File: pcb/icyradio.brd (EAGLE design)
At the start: 100 x 100 mm, 142 parts, among them J1 TRSJACK, J2 TRSJACK, J3 TRSJACK, U1 ICE40HX8K-CT256, U10 ATSAMS70Q21B-C, U2 EFM32GG11B820F2048GL120, U3 LTC2206, U4 CP2615, U5 DSC1211DE3-C0017, U6 TSCS25A3X1NDGXZAX, U7 MIC5301-1.8YD5, U8 MIC23159, U9 RT820T2, X1 8 MHz, X2 32.768 kHz, X3 DNP

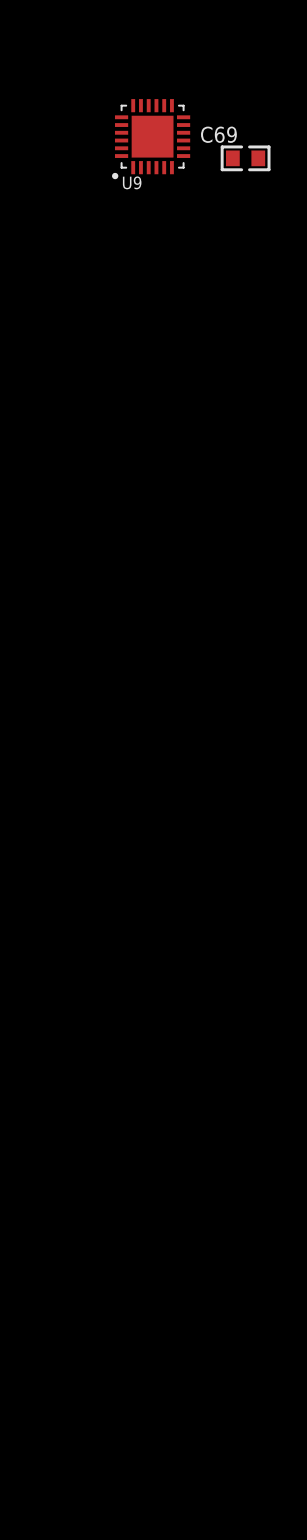
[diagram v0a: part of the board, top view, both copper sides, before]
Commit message: Added SPI slave with lots of registers Changed some names and comments Added IRQ logic
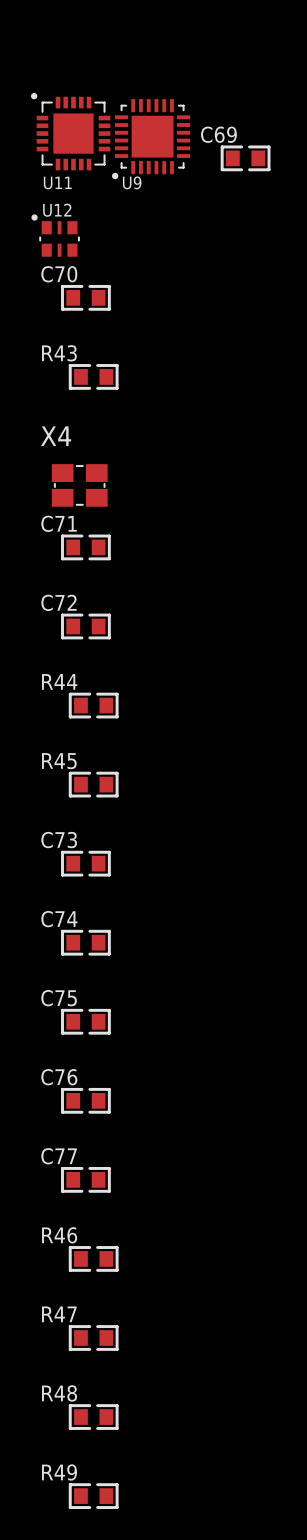
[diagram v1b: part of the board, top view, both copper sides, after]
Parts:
- added C70, C73, C74, C75, C76, C77: 100nF, Capacitor:CAP0603
- added C71, C72: DNP, Capacitor:CAP0603
- added R43, R44, R45: 100K Ohms, Resistor:RES0603
- added R46, R47, R48, R49: 0 Ohms, Resistor:RES0603
- added U11: SI5351C, Silicon Labs:QFN20
- added U12: DSC1201DE3-50M00000, Microchip:VDFN6
- added X4: DNP, Crystal:4-SMD-3225
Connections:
- new net !CLK_MNGR_IRQ: R45.1, U11.3
- new net !CLK_MNGR_OE: R44.1, U11.7
- new net !CLK_MNGR_REFCLK_STDBY: R43.2, U12.1
- new net DDC_CLK: R49.1
- new net FPGA_GP_CLK1: R48.1
- new net FPGA_GP_CLK2: R47.1
- new net MCU_MAIN_CLK: R46.1
- new net N$60: U11.6, U12.4
- new net N$61: C71.1, U11.2, X4.4
- new net N$62: C72.1, U11.1, X4.2
- net 3V3: now also C70.1, C73.1, C74.1, C75.1, C76.1, C77.1, R44.2, R45.2, U11.10, U11.11, U11.14, U11.18, U11.20, U12.6
- net GND: now also C70.2, C71.2, C72.2, C73.2, C74.2, C75.2, C76.2, C77.2, R43.1, U11.21, U12.3, X4.1, X4.3

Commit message: Add testbenches Change toolchain flow
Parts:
- added C100, C101, C102, C103, C98, C99: 220pF, Capacitor:CAP0603
- added C104, C105, C106, C108, C109, C111, C112, C113, C117, C121, C122, C126, C128, C131, C78, C79, C80, C81, C82, C83, C97: 100nF, Capacitor:CAP0603
- added C107, C110: DNP, Capacitor:CAP0603
- added C114, C115, C129, C133, C134, C140, C141, C84, C87, C88: 4.7uF, Capacitor:CAP0603
- added C116, C119, C124: 470pF, Capacitor:CAP0603
- added C118, C123, C125, C127: 100uF, Capacitor:CAP1206
- added C120, C130, C85, C86: 10nF, Capacitor:CAP0603
- added C132, C135, C136, C138, C139, C89, C90, C91, C92, C95, C96: 1uF, Capacitor:CAP0603
- added C137: 10uF, Capacitor:CAP0603
- added C93, C94: 22nF, Capacitor:CAP0603
- added L10, L11, L12, L7, L8, L9: 1.3uH, Inductor:IND0603
- added L13, L14: (no value), Inductor:IND0603
- added L15, L16, L17, L18: 2.7nH, Inductor:IND0603
- added L19: 2.2uH, Inductor:IND0805
- added L20, L22: 2.2uH, Inductor:IND2520
- added L21: 350nH, Inductor:IND0805
- added L23: 350nH, Inductor:IND0603
- added R50, R51, R62, R63, R66, R69, R71, R72, R73: 100K Ohms, Resistor:RES0603
- added R52, R53, R54, R55, R56, R57: 0 Ohms, Resistor:RES0603
- added R58, R59: 5.1K Ohms, Resistor:RES0603
- added R60: 274K Ohms, Resistor:RES0603
- added R61: 294K Ohms, Resistor:RES0603
- added R64, R67: 309K Ohms, Resistor:RES0603
- added R65: 64.9K Ohms, Resistor:RES0603
- added R68: 71.5K Ohms, Resistor:RES0603
- added R70: 820 Ohms, Resistor:RES0603
- added RFCON2: RFCON-SMA-EDGE, RF Connector:SMA-EDGE
- added RFCON3: RFCON-U.FL, RF Connector:U.FL
- added U13: DSC1201DE3-50M00000, Microchip:VDFN6
- added U14: SI5351C, Silicon Labs:QFN20
- added U15: MIC23155, Microchip:DFN10
- added U16: MIC23159, Microchip:VQFN20
- added U17: MIC2019, Microchip:SOT23-6
- added U18: ADP150UJZ-1.8, Analog Devices:SOT23-5
- added U19: ADP150UJZ-3.3, Analog Devices:SOT23-5
- added U20, U21: MIC94305, Microchip:DFN6
- C10: value 4.7uF -> 2.2uF
- C11, C56: value 10nF -> 100nF
- C12: value 1uF -> 12pF
- C13: value 100nF -> 12pF
- C14: value 330pF -> 12pF
- C15: value 6.8nF -> 1uF
- C17, C18: value DNP -> 100nF
- C19: value 100nF -> 6.8nF
- C2, C3, C4: value 12pF -> 100nF
- C21: value 100nF -> 2.2uF
- C24, C28: value 100nF -> 330pF
- C29: value 2.2uF -> 10nF
- C30, C42, C55, C57: value 1uF -> 100nF
- C33: value 100nF -> 1uF
- C37, C38, C39, C58: value 4.7uF -> 100nF
- C41: value 10nF -> 100pF
- C43, C44, C51, C52: value 220pF -> 200pF
- C45, C46: value 1uF -> 200pF
- C47, C50: value 1uF -> 620pF
- C48, C49: value 220pF -> 620pF
- C53, C54: value 22nF -> 200pF
- C6: value 2.2uF -> 100nF
- C60, C66: value 100uF -> 100nF; device Capacitor:CAP1206 -> Capacitor:CAP0603
- C61: value 470pF -> 10nF
- C62: value 470pF -> 100nF
- C63: value 4.7uF -> 10pF
- C65, C67: value 100nF -> 10pF
- C68: value 100uF -> 0.4pF; device Capacitor:CAP1206 -> Capacitor:CAP0603
- C69, C75, C76: value 100nF -> 0.4pF
- C70: value 100nF -> 2.7nF
- C71: value DNP -> 39nF
- C72: value DNP -> 1.3pF
- C73: value 100nF -> 1.3pF
- C74: value 100nF -> 1.2nF
- C8: value 100nF -> DNP
- C9: value 330pF -> DNP
- L1: value 4.7uH -> 150nH
- L3: value 150nH -> 8.2nH
- L4: value 8.2nH -> 680nH
- L5: value 2.2uH -> 1.3uH; device Inductor:IND0805 -> Inductor:IND0603
- L6: value 2.2uH -> 1.3uH; device Inductor:IND2520 -> Inductor:IND0603
- R1: value 25 Ohms -> 100K Ohms
- R11: value 1K Ohms -> 220 Ohms
- R12: value 10K Ohms -> 220 Ohms
- R13: value 5.1K Ohms -> 100K Ohms
- R14: value 5.1K Ohms -> 1.5K Ohms
- R15: value 47K Ohms -> 50 Ohms
- R16: value 24K Ohms -> 50 Ohms
- R17, R18: value 10K Ohms -> 50 Ohms
- R2: value 25 Ohms -> 0 Ohms
- R20: value 4.7K Ohms -> 10K Ohms
- R21, R22: value 600 Ohms -> 100 Ohms
- R23: value 4.7K Ohms -> 100K Ohms
- R24: value 2.21K Ohms -> 4.7K Ohms
- R25: value 2.21K Ohms -> 100 Ohms
- R26: value 4.7K Ohms -> 360 Ohms
- R27: value 600 Ohms -> 680 Ohms
- R28: value 600 Ohms -> 5.1K Ohms
- R29: value 4.7K Ohms -> 5.1K Ohms
- R3: value 25 Ohms -> 1K Ohms
- R30: value 3.57 Ohms -> 10K Ohms
- R31: value 3.57 Ohms -> 24K Ohms
- R32: value 100 Ohms -> 47K Ohms
- R33: value 100 Ohms -> 10K Ohms
- R34: value 309K Ohms -> 100 Ohms
- R35: value 71.5K Ohms -> 2.21K Ohms
- R36, R40: value 100K Ohms -> 4.7K Ohms
- R37: value 274K Ohms -> 4.7K Ohms
- R38: value 294K Ohms -> 10K Ohms
- R39: value 100K Ohms -> 2.21K Ohms
- R41: value 5.1K Ohms -> 4.7K Ohms
- R42: value 5.1K Ohms -> 100 Ohms
- R43, R44: value 100K Ohms -> 600 Ohms
- R45: value 100K Ohms -> 3.57 Ohms
- R46, R47: value 0 Ohms -> 600 Ohms
- R48: value 0 Ohms -> 3.57 Ohms
- R49: value 0 Ohms -> 100K Ohms
- R5: value 220 Ohms -> 25 Ohms
- R6: value 220 Ohms -> 1.8K Ohms
- R7: value DNP -> 25 Ohms
- R8: value 1.8K Ohms -> 25 Ohms
- R9: value 0 Ohms -> DNP
- U1: value ICE40HX8K-CT256 -> EFM32GG11B420F2048GL112; device Lattice:CABGA256 -> EFM32:BGA112
- U10: value ATSAMS70Q21B-C -> ADF4351; device Microchip:LFBGA144 -> Analog Devices:QFN32
- U11: value SI5351C -> TSCS25A3X1NDGXZAX; device Silicon Labs:QFN20 -> Tempo Semiconductor:QFN40
- U12: value DSC1201DE3-50M00000 -> CP2615; device Microchip:VDFN6 -> Silicon Labs:QFN32
- U2: value EFM32GG11B820F2048GL120 -> ATSAMS70Q21B-C; device EFM32:BGA120 -> Microchip:LFBGA144
- U3: value LTC2206 -> ICE40HX8K-CT256; device Analog Devices:QFN48 -> Lattice:CABGA256
- U4: value CP2615 -> DSC1211DE3-C0017; device Silicon Labs:QFN32 -> Microchip:VDFN6
- U5: value DSC1211DE3-C0017 -> LTC2206; device Microchip:VDFN6 -> Analog Devices:QFN48
- U6: value TSCS25A3X1NDGXZAX -> RT820T2; device Tempo Semiconductor:QFN40 -> Rafael Micro:QFN24
- U7: value MIC5301-1.8YD5 -> ADL5385; device Microchip:SOT23-5 -> Analog Devices:QFN24
- U8: value MIC23159 -> AD9117; device Microchip:VQFN20 -> Analog Devices:QFN40
- U9: value RT820T2 -> ADL5545; device Rafael Micro:QFN24 -> Analog Devices:SOT89
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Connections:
- net TUNER_IF_VAGC renamed RXTUNER_IF_VAGC
- removed net !IFADC_OE: U3.44
- removed net 1V2_EN: R40.2, U8.18
- removed net CODEC_1V8: C34.1, C35.1, C36.1, C55.1, U6.17, U6.3, U6.33, U6.37, U7.5
- removed net DDC_CLK: R49.1
- removed net IFADC_CLK: U3.10
- removed net IFADC_D0: U3.18
- removed net IFADC_D1: U3.19
- removed net IFADC_D10: U3.34
- removed net IFADC_D11: U3.35
- removed net IFADC_D12: U3.39
- removed net IFADC_D13: U3.40
- removed net IFADC_D14: U3.41
- removed net IFADC_D15: U3.42
- removed net IFADC_D2: U3.20
- removed net IFADC_D3: U3.21
- removed net IFADC_D4: U3.22
- removed net IFADC_D5: U3.26
- removed net IFADC_D6: U3.27
- removed net IFADC_D7: U3.28
- removed net IFADC_D8: U3.32
- removed net IFADC_D9: U3.33
- removed net IFADC_DITH: U3.17
- removed net IFADC_GAIN: U3.47
- removed net IFADC_OF: U3.43
- removed net IFADC_SHDN: R12.2, U3.16
- removed net IFADC_VCM: C5.1, C6.1, R2.2, R3.1, TRF1.2, U3.2
- removed net MCU_DVDD: C10.1, L1.1, U2.H11
- removed net MCU_MAIN_CLK: R46.1
- removed net TUNER_IFN: R5.1, U9.12
- removed net TUNER_IFP: R6.1, U9.13
- removed net TUNER_REFCLK_SEL: U5.1
- new net !RXADC_OE: U5.44
- new net !TXPA_OC: R73.1, U17.4
- new net 1V8_ANA_CODEC_CLEAN: C138.1, C80.1, C82.1, C83.1, U11.17, U11.3, U11.33, U11.37, U18.5
- new net 3V3_ANA_RX_CLEAN: C10.1, C141.1, C16.1, C18.1, C2.1, C20.1, C22.1, C4.1, C6.1, R3.1, U21.1, U21.2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
- new net 3V3_ANA_RX_CLEAN_EN: R72.2, U21.4
- new net 3V3_ANA_TXPLL_CLEAN: C139.1, C55.1, C56.1, C57.1, C58.1, C60.1, L13.1, L14.2, U10.10, U10.16, U10.17, U10.32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
- new net 3V3_ANA_TX_CLEAN: C140.1, C34.1, C36.1, U20.1, U20.2, U8.26
- new net 3V3_ANA_TX_CLEAN_EN: R71.2, U20.4
- new net 3V3_FB1: R64.1, R65.2, U15.4
- new net 3V6_ANA: C121.1, C123.1, C133.1, C134.1, C135.1, C136.1, L20.2, R64.2, U15.3, U18.1, U18.3, U19.1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
- new net 3V6_ANA_PGOOD: R63.1, U15.5
- new net 5V0_ANA_TXMIXER_CLEAN: C131.1, C132.1, C30.1, C31.1, C32.1, L23.2, U17.1, U7.11, U7.23, U7.24, U7.8, U7.9
- new net 5V0_ANA_TXPA_CLEAN: C137.1, C39.1, C41.1, L4.2, U17.6
- new net DSP_MCU_MAIN_CLK: R54.1
- new net FPGA_DDC_CLK: R52.1
- new net FPGA_GP_CLK3: R56.1
- new net N$63: C42.2, RFCON2.SIG
- new net N$64: C35.1, U7.7
- new net N$65: L20.1, U15.1
- new net N$66: C116.1, U15.6
- new net N$67: C69.2, L14.1, L16.1, R25.1, U10.13
- new net N$68: C73.2, L16.2, L18.1
- new net N$69: C68.1, L13.2, L15.1, R25.2, U10.12
- new net N$70: C72.1, L15.2, L17.1
- new net N$71: C75.1, C77.1, L17.2
- new net N$72: C76.2, C78.1, L18.2
- new net N$73: C44.2, L6.1, R16.1, U8.29
- new net N$74: C43.1, L5.1, R15.2, U8.28
- new net N$75: C48.2, L10.1, L6.2
- new net N$76: C47.1, L5.2, L9.1
- new net N$77: C33.1, U8.7
- new net N$78: C70.1, C71.1, R27.2, U10.7
- new net N$79: C74.1, R27.1, U10.20
- new net N$80: C46.2, L8.1, R18.1, U8.22
- new net N$81: C45.1, L7.1, R17.2, U8.23
- new net N$82: C50.2, L12.1, L8.2
- new net N$83: C49.1, L11.1, L7.2
- new net N$84: C71.2, R26.2
- new net N$85: C66.1, C67.1, U10.19
- new net N$86: C64.1, C65.1, U10.23
- new net N$87: C62.1, C63.1, U10.24
- new net N$88: R24.2, U10.22
- new net N$89: C61.2, U10.29
- new net N$90: C40.2, C42.1, L4.1, U9.3
- new net N$92: C40.1, R14.1
- new net N$93: C120.1, D3.2, F1.1, L21.1
- new net N$94: R70.2, U17.5
- new net RXADC_CLK: U5.10
- new net RXADC_D0: U5.18
- new net RXADC_D1: U5.19
- new net RXADC_D10: U5.34
- new net RXADC_D11: U5.35
- new net RXADC_D12: U5.39
- new net RXADC_D13: U5.40
- new net RXADC_D14: U5.41
- new net RXADC_D15: U5.42
- new net RXADC_D2: U5.20
- new net RXADC_D3: U5.21
- new net RXADC_D4: U5.22
- new net RXADC_D5: U5.26
- new net RXADC_D6: U5.27
- new net RXADC_D7: U5.28
- new net RXADC_D8: U5.32
- new net RXADC_D9: U5.33
- new net RXADC_DITH: U5.17
- new net RXADC_GAIN: U5.47
- new net RXADC_OF: U5.43
- new net RXADC_SHDN: R1.1, U5.16
- new net RXADC_VCM: C21.1, C23.1, R7.1, R8.2, TRF1.2, U5.2
- new net RXTUNER_IFN: R12.1, U6.12
- new net RXTUNER_IFP: R11.1, U6.13
- new net RXTUNER_REFCLK_SEL: U4.1
- new net SMC_MCU_MAIN_CLK: R57.1
- new net TXDAC_AUXI: R19.2, U8.33
- new net TXDAC_AUXQ: R20.2, U8.32
- new net TXDAC_D0: U8.15
- new net TXDAC_D1: U8.14
- new net TXDAC_D10: U8.2
- new net TXDAC_D11: U8.1
- new net TXDAC_D12: U8.40
- new net TXDAC_D13: U8.39
- new net TXDAC_D2: U8.13
- new net TXDAC_D3: U8.12
- new net TXDAC_D4: U8.11
- new net TXDAC_D5: U8.10
- new net TXDAC_D6: U8.9
- new net TXDAC_D7: U8.8
- new net TXDAC_D8: U8.4
- new net TXDAC_D9: U8.3
- new net TXPA_BIAS_EN: R69.2, U17.3
- new net TXPLL_EN: R23.2, U10.4
- new net TX_MIXER_EN: R13.2, U7.12
- new net TX_MIXER_IBBN: C52.2, L10.2, R19.1, R21.1, U7.14
- new net TX_MIXER_IBBP: C51.1, L9.2, R21.2, U7.13
- new net TX_MIXER_LON: C78.2, U7.22
- new net TX_MIXER_LOP: C77.2, U7.21
- new net TX_MIXER_QBBN: C54.2, L12.2, R20.1, R22.1, U7.17
- new net TX_MIXER_QBBP: C53.1, L11.2, R22.2, U7.18
- net !CLK_MNGR_IRQ: now also R51.1, U14.3; no longer R45.1, U11.3
- net !CLK_MNGR_OE: now also R50.1, U14.7; no longer R44.1, U11.7
- net !CLK_MNGR_REFCLK_STDBY: now also R49.2, U13.1; no longer R43.2, U12.1
- net !CODEC_RST: now also R30.1, U11.7; no longer R19.1, U6.7
- net !I2S_BRG_CFG: now also R33.1, U12.21; no longer R18.1, U4.21
- net !I2S_BRG_RST: now also R38.1, U12.9; no longer R17.1, U4.9
- net 1V2: now also C117.1, C118.1, L19.1, R60.2, U16.17, U3.A14, U3.E12, U3.E8, U3.F10, U3.F6, U3.K10, U3.K6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; no longer C65.1, C66.1, L5.1, R37.2, U1.A14, U1.E12, U1.E8, U1.F10, U1.F6, U1.K10, U1.K6, U1.L2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
- net 1V2_PGOOD: now also R62.1, U16.15; no longer R39.1, U8.15
- net 3V3: now also C104.1, C105.1, C106.1, C108.1, C109.1, C111.1, C126.1, C127.1, C37.1, C5.1, C59.1, C7.1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; no longer C19.1, C20.1, C21.1, C22.1, C23.1, C25.1, C26.1, C27.1, C28.1, C29.1, C30.1, C31.1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
- net 3V3_FB: now also R67.1, R68.2, U16.11; no longer R34.1, R35.2, U8.11
- net 3V3_PGOOD: now also R66.1, U16.12; no longer R36.1, U8.12
- net 4V2_FB: now also R60.1, R61.2, U16.16; no longer R37.1, R38.2, U8.16
- net 5V0: now also C112.1, C113.1, C114.1, C115.1, C122.1, C125.1, C128.1, C129.1, C130.1, L21.2, L23.1, U15.2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; no longer C58.1, C59.1, C60.1, C63.1, C64.1, D3.2, F1.1, U8.1, U8.20, U8.6, U8.7, U8.9
- net BRG_I2S_LRCLK: now also U12.28; no longer U4.28
- net BRG_I2S_MCLK: now also U12.26; no longer U4.26
- net BRG_I2S_SCLK: now also U12.2; no longer U4.2
- net BRG_I2S_SDIN: now also U12.1; no longer U4.1
- net BRG_I2S_SDOUT: now also U12.32; no longer U4.32
- net CODEC_HP_L: now also C103.1, R48.1; no longer C52.1, R31.1
- net CODEC_HP_R: now also C100.1, R45.1; no longer C51.1, R30.1
- net CODEC_I2S_LRCLK: now also U11.15, U11.19; no longer U6.15, U6.19
- net CODEC_I2S_MCLK: now also U11.6; no longer U6.6
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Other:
- board size 100 x 100 mm -> 150 x 100 mm

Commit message: Huge PCB layout progress
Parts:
- removed C1, C132, C135, C136, C138, C139, C15, C33, C89, C90, C91, C92, C95, C96: 1uF, Capacitor:CAP0603
- removed C10, C21: 2.2uF, Capacitor:CAP0603
- removed C100, C98, C99: 220pF, Capacitor:CAP0603
- removed C11, C112, C113, C117, C121, C122, C126, C128, C131, C16, C17, C18, C2, C20, C22, C23, C25, C26, C27, C3, C30, C31, C32, C34, C35, C36, C37, C38, C39, C4, C42, C5, C55, C56, C57, C58, C59, C6, C60, C62, C64, C66, C7, C77, C78, C79, C80, C81, C82, C83, C97: 100nF, Capacitor:CAP0603
- removed C114, C115, C129, C133, C134, C140, C141, C84, C87, C88: 4.7uF, Capacitor:CAP0603
- removed C116, C119, C124: 470pF, Capacitor:CAP0603
- removed C118, C123, C125, C127: 100uF, Capacitor:CAP1206
- removed C12, C13, C14: 12pF, Capacitor:CAP0603
- removed C120, C130, C29, C40, C61, C85, C86: 10nF, Capacitor:CAP0603
- removed C137: 10uF, Capacitor:CAP0603
- removed C19: 6.8nF, Capacitor:CAP0603
- removed C24, C28: 330pF, Capacitor:CAP0603
- removed C41: 100pF, Capacitor:CAP0603
- removed C43, C44, C45, C46, C51, C52, C53, C54: 200pF, Capacitor:CAP0603
- removed C47, C48, C49, C50: 620pF, Capacitor:CAP0603
- removed C63, C65, C67: 10pF, Capacitor:CAP0603
- removed C68, C69, C75, C76: 0.4pF, Capacitor:CAP0603
- removed C70: 2.7nF, Capacitor:CAP0603
- removed C71: 39nF, Capacitor:CAP0603
- removed C72, C73: 1.3pF, Capacitor:CAP0603
- removed C74: 1.2nF, Capacitor:CAP0603
- removed C8, C9: DNP, Capacitor:CAP0603
- removed C93, C94: 22nF, Capacitor:CAP0603
- removed D1: BAV99, Generic Diode:SOT23
- removed D2, D3: SP0503BAHT, TVS:SOT143
- removed F1: (no value), PTC Fuses:1206
- removed J1, J2, J3: TRSJACK, DC Jack:3.5TRSJACK
- removed L1, L2: 150nH, Inductor:IND0603
- removed L10, L11, L12, L5, L6, L7, L8, L9: 1.3uH, Inductor:IND0603
- removed L13, L14: (no value), Inductor:IND0603
- removed L15, L16, L17, L18: 2.7nH, Inductor:IND0603
- removed L19: 2.2uH, Inductor:IND0805
- removed L20, L22: 2.2uH, Inductor:IND2520
- removed L21: 350nH, Inductor:IND0805
- removed L23: 350nH, Inductor:IND0603
- removed L3: 8.2nH, Inductor:IND0603
- removed L4: 680nH, Inductor:IND0603
- removed R10, R19, R20, R30, R33, R38: 10K Ohms, Resistor:RES0603
- removed R11, R12: 220 Ohms, Resistor:RES0603
- removed R13, R23, R49, R50, R51, R62, R63, R66, R69, R71, R72, R73: 100K Ohms, Resistor:RES0603
- removed R14: 1.5K Ohms, Resistor:RES0603
- removed R15, R16, R17, R18: 50 Ohms, Resistor:RES0603
- removed R21, R22, R25, R34, R42: 100 Ohms, Resistor:RES0603
- removed R24, R36, R37, R40, R41: 4.7K Ohms, Resistor:RES0603
- removed R26: 360 Ohms, Resistor:RES0603
- removed R27: 680 Ohms, Resistor:RES0603
- removed R28, R29, R58, R59: 5.1K Ohms, Resistor:RES0603
- removed R31: 24K Ohms, Resistor:RES0603
- removed R32: 47K Ohms, Resistor:RES0603
- removed R35, R39: 2.21K Ohms, Resistor:RES0603
- removed R43, R44, R46, R47: 600 Ohms, Resistor:RES0603
- removed R45, R48: 3.57 Ohms, Resistor:RES0603
- removed R52, R53, R54, R55, R56, R57: 0 Ohms, Resistor:RES0603
- removed R60: 274K Ohms, Resistor:RES0603
- removed R61: 294K Ohms, Resistor:RES0603
- removed R64, R67: 309K Ohms, Resistor:RES0603
- removed R65: 64.9K Ohms, Resistor:RES0603
- removed R68: 71.5K Ohms, Resistor:RES0603
- removed R7, R8: 25 Ohms, Resistor:RES0603
- removed R70: 820 Ohms, Resistor:RES0603
- removed R9: DNP, Resistor:RES0603
- removed RFCON1, RFCON2: RFCON-SMA-EDGE, RF Connector:SMA-EDGE
- removed RFCON3: RFCON-U.FL, RF Connector:U.FL
- removed TC1: TC2050-IDC, TagConnect:TC2050-IDC
- removed TRF1: ETC1-1T-2TR, Inductor:TRF-SM-22
- removed U1: EFM32GG11B420F2048GL112, EFM32:BGA112
- removed U10: ADF4351, Analog Devices:QFN32
- removed U11: TSCS25A3X1NDGXZAX, Tempo Semiconductor:QFN40
- removed U12: CP2615, Silicon Labs:QFN32
- removed U13: DSC1201DE3-50M00000, Microchip:VDFN6
- removed U14: SI5351C, Silicon Labs:QFN20
- removed U15: MIC23155, Microchip:DFN10
- removed U16: MIC23159, Microchip:VQFN20
- removed U17: MIC2019, Microchip:SOT23-6
- removed U18: ADP150UJZ-1.8, Analog Devices:SOT23-5
- removed U19: ADP150UJZ-3.3, Analog Devices:SOT23-5
- removed U2: ATSAMS70Q21B-C, Microchip:LFBGA144
- removed U20, U21: MIC94305, Microchip:DFN6
- removed U3: ICE40HX8K-CT256, Lattice:CABGA256
- removed U4: DSC1211DE3-C0017, Microchip:VDFN6
- removed U5: LTC2206, Analog Devices:QFN48
- removed U6: RT820T2, Rafael Micro:QFN24
- removed U7: ADL5385, Analog Devices:QFN24
- removed U8: AD9117, Analog Devices:QFN40
- removed U9: ADL5545, Analog Devices:SOT89
- removed USB1, USB2: USB-C-16P-SMD-FLAT-SIDE-TYPE-2, USB Connector:USB-C-16P-SMD-FLAT-SIDE-TYPE-2
- removed X1: 8 MHz, Crystal:2-SMD-5032
- removed X2: 32.768 kHz, Crystal:2-SMD-3215
- removed X3, X4: DNP, Crystal:4-SMD-3225
- added C201, C417, C504, C712, C713, C714, C715, C718, C719, C921, C924, C925, C927, C928: 1uF, Capacitor:CAP0603
- added C202, C203, C204, C205, C206, C207, C208, C209, C210, C211, C212, C213, C214, C215, C216, C301, C302, C303, C304, C305, C306, C307, C308, C309, C310, C311, C312, C313, C314, C315, C316, C317, C318, C401, C402, C403, C404, C405, C406, C407, C408, C409, C413, C418, C419, C420, C422, C424, C425, C427, C428, C429, C501, C502, C503, C505, C506, C507, C508, C509, C513, C601, C602, C603, C604, C605, C606, C607, C609, C611, C622, C623, C701, C702, C703, C704, C705, C706, C720, C801, C802, C803, C805, C808, C901, C902, C906, C910, C911, C915, C917, C920: 100nF, Capacitor:CAP0603
- added C217, C707, C710, C711, C903, C904, C918, C922, C923, C929, C930: 4.7uF, Capacitor:CAP0603
- added C218, C608, C610, C612: 10pF, Capacitor:CAP0603
- added C410, C411, C511, C804, C807: DNP, Capacitor:CAP0603
- added C412, C423: 2.2uF, Capacitor:CAP0603
- added C414, C415, C416: 12pF, Capacitor:CAP0603
- added C421: 6.8nF, Capacitor:CAP0603
- added C426, C430: 330pF, Capacitor:CAP0603
- added C431, C708, C709, C909, C919: 10nF, Capacitor:CAP0603
- added C510, C619: 1.2nF, Capacitor:CAP0603
- added C512: 68pF, Capacitor:CAP0603
- added C514, C515, C516, C517, C522, C523, C524, C525: 200pF, Capacitor:CAP0603
- added C518, C519, C520, C521: 620pF, Capacitor:CAP0603
- added C613, C614, C620, C621: 0.4pF, Capacitor:CAP0603
- added C615: 39nF, Capacitor:CAP0603
- added C616: 2.7nF, Capacitor:CAP0603
- added C617, C618: 1.3pF, Capacitor:CAP0603
- added C716, C717: 22nF, Capacitor:CAP0603
- added C721, C722, C723, C724, C725, C726: 220pF, Capacitor:CAP0603
- added C905, C908, C913: 470pF, Capacitor:CAP0603
- added C907, C912, C914, C916: 100uF, Capacitor:CAP1206
- added C926: 10uF, Capacitor:CAP0603
- added D401: BAV99, Generic Diode:SOT23
- added D701, D901: SP0503BAHT, TVS:SOT143
- added F901: (no value), PTC Fuses:1206
- added J701, J702, J703: TRSJACK, DC Jack:3.5TRSJACK
- added L201, L202: 470 Ohms, Inductor:IND0603
- added L203: 10uH, Inductor:IND0603
- added L401, L402: 150nH, Inductor:IND0603
- added L403: 8.2nH, Inductor:IND0603
- added L501: 470nH, Inductor:IND0603
- added L502, L503, L504, L505, L506, L507, L508, L509: 1.3uH, Inductor:IND0603
- added L601, L602: 19nH, Inductor:IND0603
- added L603, L604, L605, L606: 2.7nH, Inductor:IND0603
- added L901: 2.2uH, Inductor:IND0805
- added L902, L904: 2.2uH, Inductor:IND2520
- added L903: 350nH, Inductor:IND0805
- added L905: 350nH, Inductor:IND0603
- added R201: 5.62K Ohms, Resistor:RES0603
- added R202: 2.2 Ohms, Resistor:RES0603
- added R301, R401, R501, R601, R801, R802, R803, R905, R906, R909, R912, R914: 100K Ohms, Resistor:RES0603
- added R402, R804, R805, R806, R807, R808, R809: 0 Ohms, Resistor:RES0603
- added R403: 1K Ohms, Resistor:RES0603
- added R404, R405, R407, R408: 25 Ohms, Resistor:RES0603
- added R406: 1.8K Ohms, Resistor:RES0603
- added R409, R502, R503, R604: DNP, Resistor:RES0603
- added R410, R508, R509, R703, R706, R711: 10K Ohms, Resistor:RES0603
- added R411, R412: 220 Ohms, Resistor:RES0603
- added R504, R505, R506, R507: 50 Ohms, Resistor:RES0603
- added R510, R511, R603, R707, R715: 100 Ohms, Resistor:RES0603
- added R602: 5.1K Ohm, Resistor:RES0603
- added R605: 360 Ohms, Resistor:RES0603
- added R606: 680 Ohms, Resistor:RES0603
- added R701, R702, R901, R902: 5.1K Ohms, Resistor:RES0603
- added R704: 24K Ohms, Resistor:RES0603
- added R705: 47K Ohms, Resistor:RES0603
- added R708, R712: 2.21K Ohms, Resistor:RES0603
- added R709, R710, R713, R714: 4.7K Ohms, Resistor:RES0603
- added R716, R717, R719, R720: 600 Ohms, Resistor:RES0603
- added R718, R721: 3.57 Ohms, Resistor:RES0603
- added R903: 274K Ohms, Resistor:RES0603
- added R904: 294K Ohms, Resistor:RES0603
- added R907, R910: 309K Ohms, Resistor:RES0603
- added R908: 64.9K Ohms, Resistor:RES0603
- added R911: 71.5K Ohms, Resistor:RES0603
- added R913: 820 Ohms, Resistor:RES0603
- added RFCON401, RFCON501: RFCON-SMA-EDGE, RF Connector:SMA-EDGE
- added RFCON502: RFCON-U.FL, RF Connector:U.FL
- added TC101, TC201: TC2050-IDC, TagConnect:TC2050-IDC
- added TRF401: ETC1-1T-2TR, Inductor:TRF-SM-22
- added U$1: (no value), Silkscreen:JS_10MM
- added U$2: (no value), Silkscreen:RADIO_10MM
- added U101: EFM32GG11B420F2048GL112, EFM32:BGA112
- added U201: ATSAMS70Q21B-C, Microchip:LFBGA144
- added U301: ICE40HX8K-CT256, Lattice:CABGA256
- added U401: DSC1211DE3-C0017, Microchip:VDFN6
- added U402: LTC2206, Analog Devices:QFN48
- added U403: RT820T2, Rafael Micro:QFN24
- added U501: ADL5385, Analog Devices:QFN24
- added U502: AD9117, Analog Devices:QFN40
- added U503: ADL5601, Analog Devices:SOT89
- added U601, U801: DSC1201DE3-50M00000, Microchip:VDFN6
- added U602: ADF4351, Analog Devices:QFN32
- added U701: TSCS25A3X1NDGXZAX, Tempo Semiconductor:QFN40
- added U702: CP2615, Silicon Labs:QFN32
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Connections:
- removed net !RST: TC1.10
- removed net 1V8_ANA_CODEC_CLEAN: C138.1, C80.1, C82.1, C83.1, U11.17, U11.3, U11.33, U11.37, U18.5
- removed net 3V3_ANA_RX_CLEAN_EN: R72.2, U21.4
- removed net 3V3_ANA_TX_CLEAN_EN: R71.2, U20.4
- removed net 3V3_FB1: R64.1, R65.2, U15.4
- removed net 4V2_FB: R60.1, R61.2, U16.16
- removed net DSP_MCU_MAIN_CLK: R54.1
- removed net MAIN_HFXTAL_N: U1.L9, X1.1
- removed net MAIN_HFXTAL_P: U1.L8, X1.2
- removed net MAIN_LFXTAL_N: U1.L1, X2.2
- removed net MAIN_LFXTAL_P: U1.K1, X2.1
- removed net MCU_D+: D3.4, USB2.A6, USB2.B6
- removed net MCU_D-: D3.3, USB2.A7, USB2.B7
- removed net N$20: C15.1, U6.4
- removed net N$21: C24.1, R6.1, U6.15
- removed net N$23: C11.1, U6.17
- removed net N$24: C9.1, U6.9, X3.4
- removed net N$25: C8.1, R2.1, U6.8, X3.2
- removed net SMC_MCU_MAIN_CLK: R57.1
- removed net SWCLK: TC1.4
- removed net SWDIO: TC1.2
- removed net SWO: TC1.6
- removed net TX_MIXER_EN: R13.2, U7.12
- removed net TX_MIXER_IBBN: C52.2, L10.2, R19.1, R21.1, U7.14
- removed net TX_MIXER_IBBP: C51.1, L9.2, R21.2, U7.13
- removed net TX_MIXER_LON: C78.2, U7.22
- removed net TX_MIXER_LOP: C77.2, U7.21
- removed net TX_MIXER_QBBN: C54.2, L12.2, R20.1, R22.1, U7.17
- removed net TX_MIXER_QBBP: C53.1, L11.2, R22.2, U7.18
- new net !DSP_IRQ: U101.B2, U201.K12
- new net !DSP_RESET: TC201.10, U201.H12
- new net !DSP_SPI_SS: U101.D1, U201.J2
- new net !FPGA_CRESET: R301.2, U101.G2, U301.N11
- new net !FPGA_SPI_CS: U101.H1, U301.R12
- new net !FPGA_SRESET: U101.E2, U301.H16
- new net !SMC_RESET: TC101.10, U101.K6
- new net !TXDAC_CS: R2.1, U101.A4, U502.38
- new net !TXPLL_MUTE: R4.2, U101.B6, U602.26
- new net 1V2_FB: R903.1, R904.2, U902.16
- new net 1V8_CODEC_CLEAN: C702.1, C704.1, C705.1, C927.1, U701.17, U701.3, U701.33, U701.37, U904.5
- new net 3V6_ANA_FB: R907.1, R908.2, U901.4
- new net CLK_MNGR_I2C_SCL: R6.1, U101.B9, U802.4
- new net CLK_MNGR_I2C_SDA: R5.1, U101.A9, U802.5
- new net DSP_BB_I2S_LRCLK: U201.C2, U301.D15
- new net DSP_BB_I2S_SCLK: U201.H3, U301.E16
- new net DSP_BB_I2S_SDIN: U201.B1, U301.D16
- new net DSP_BB_I2S_SDOUT: U201.A1, U301.C16
- new net DSP_D+: D901.4, U201.A4, USB901.A6, USB901.B6
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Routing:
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- added copper zone on layer 1, net 1V2
- added copper zone on layer 15, net 1V2
- added copper zone on layer 15, net 1V8_CODEC_CLEAN
- added copper zone on layer 1, net 3V3
- added copper zone on layer 15, net 3V3
- added copper zone on layer 15, net 3V3_ANA_RX_CLEAN
- added copper zone on layer 15, net 3V3_ANA_TXPLL_CLEAN
- added copper zone on layer 15, net 3V3_ANA_TX_CLEAN
- added copper zone on layer 1, net 3V6_ANA
- added copper zone on layer 15, net 3V6_ANA
- added copper zone on layer 1, net 5V0_ANA_TXMIXER_CLEAN
- added copper zone on layer 15, net 5V0_ANA_TXMIXER_CLEAN
- added copper zone on layer 1, net GND
- added copper zone on layer 15, net GND
- added copper zone on layer 16, net GND
- added copper zone on layer 2, net GND
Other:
- outline, holes or cut-outs redrawn
- board text added: "ilva"

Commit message: Nothing to do
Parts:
- removed C802, C803, C805, C808: 100nF, Capacitor:CAP0603
- removed C804, C807: DNP, Capacitor:CAP0603
- removed R1, R2, R4, R914: 100K Ohms, Resistor:RES0603
- removed R3, R806, R807, R808, R809: 0 Ohms, Resistor:RES0603
- removed R5, R6: 4.7K Ohms, Resistor:RES0603
- removed U802: SI5351C, Silicon Labs:QFN20
- added C1001, C1002, C1006: 100nF, Capacitor:CAP0603
- added C1003, C1004: 4.7uF, Capacitor:CAP0603
- added C1005: 470pF, Capacitor:CAP0603
- added C1007: 100uF, Capacitor:CAP1206
- added C432: 330pF, Capacitor:CAP0603
- added C433: 10nF, Capacitor:CAP0603
- added C526, C527: 200pF, Capacitor:CAP0603
- added Q801, Q802: AO3400, Alpha Omega:SOT23
- added R1001, R1002: 5.1K Ohms, Resistor:RES0603
- added R1003: 274K Ohms, Resistor:RES0603
- added R1004: 294K Ohms, Resistor:RES0603
- added R1005, R1006, R1009, R1014: 100K Ohms, Resistor:RES0603
- added R1007: 309K Ohms, Resistor:RES0603
- added R1008: 64.9K Ohms, Resistor:RES0603
- added R101, R102, R103, R104: 4.7K Ohms, Resistor:RES0603
- added R105, R203, R414, R512, R513: 10K Ohms, Resistor:RES0603
- added R413: DNP, Resistor:RES0603
- added R415, R416: 220 Ohms, Resistor:RES0603
- added R514, R515: 100 Ohms, Resistor:RES0603
- added R607: 680 Ohms, Resistor:RES0603
- added SJ1: (no value), Solder Jumper:SJ_S
- added U1001: MIC23155, Microchip:DFN10
- added U1002: MIC23159, Microchip:VQFN20
- C411, C511: value DNP -> 100nF
- C412: value 2.2uF -> DNP
- C414: value 12pF -> 2.2uF
- C415: value 12pF -> 100nF
- C417: value 1uF -> 12pF
- C419: value 100nF -> 12pF
- C420, C505: value 100nF -> 1uF
- C421: value 6.8nF -> 100nF
- C423: value 2.2uF -> 6.8nF
- C424, C427: value 100nF -> 27pF
- C425: value 100nF -> 2.2uF
- C426, C430: value 330pF -> 100nF
- C428: value 100nF -> 330pF
- C431: value 10nF -> 100nF
- C504: value 1uF -> 100nF
- C510: value 1.2nF -> 100nF
- C512: value 68pF -> 1.2nF
- C513, C906: value 100nF -> DNP
- C514: value 200pF -> 68pF
- C515: value 200pF -> 100nF
- C518, C519: value 620pF -> 200pF
- C522, C523: value 200pF -> 620pF
- C801: value 100nF -> 100uF; device Capacitor:CAP0603 -> Capacitor:CAP1206
- C903: value 4.7uF -> DNP
- C904: value 4.7uF -> 100nF
- C905: value 470pF -> 100nF
- C907: value 100uF -> 100nF; device Capacitor:CAP1206 -> Capacitor:CAP0603
- R404, R405: value 25 Ohms -> 220 Ohms
- R406: value 1.8K Ohms -> 25 Ohms
- R408: value 25 Ohms -> 4.7K Ohms
- R409: value DNP -> 1.8K Ohms
- R410: value 10K Ohms -> 4.7K Ohms
- R411, R412: value 220 Ohms -> 25 Ohms
- R502: value DNP -> 0 Ohms
- R503: value DNP -> 100K Ohms
- R504: value 50 Ohms -> 200 Ohms
- R505: value 50 Ohms -> 100K Ohms
- R506, R507: value 50 Ohms -> DNP
- R508, R509: value 10K Ohms -> 50 Ohms
- R510, R511: value 100 Ohms -> 50 Ohms
- R602: value 5.1K Ohm -> 100K Ohms
- R603: value 100 Ohms -> 5.1K Ohm
- R604: value DNP -> 100 Ohms
- R605: value 360 Ohms -> DNP
- R606: value 680 Ohms -> 360 Ohms
- R801: value 100K Ohms -> 22 Ohms
- R802: value 100K Ohms -> 10K Ohms
- R803, R905, R906, R909: value 100K Ohms -> 0 Ohms
- R805: value 0 Ohms -> 100K Ohms
- R901, R902: value 5.1K Ohms -> 100K Ohms
- R903: value 274K Ohms -> 100K Ohms
- R904: value 294K Ohms -> 0 Ohms
- R907: value 309K Ohms -> 0 Ohms
- R908: value 64.9K Ohms -> 0 Ohms
- U801: value DSC1201DE3-50M00000 -> ER-TFT035-6; device Microchip:VDFN6 -> BuyDisplay:ZIF50
- U901: value MIC23155 -> DSC1201DE3-50M00000; device Microchip:DFN10 -> Microchip:VDFN6
- U902: value MIC23159 -> SI5351C; device Microchip:VQFN20 -> Silicon Labs:QFN20
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- renumbered C908 to C1008, C909 to C1009, C910 to C1010, C911 to C1011, C912 to C1013, C913 to C1012, C914 to C1014, C915 to C1015, C916 to C1016, C917 to C1017, C918 to C1018, C919 to C1019, C920 to C1020, C921 to C1021, C922 to C1022, C923 to C1023, C924 to C1024, C925 to C1025, C926 to C1026, C927 to C1027, C928 to C1028, C929 to C1029, C930 to C1030, D901 to D1001, F901 to F1001, L901 to L1001, L902 to L1002, L903 to L1003, L904 to L1004, L905 to L1005, R910 to R1010, R911 to R1011, R912 to R1012, R913 to R1013, U903 to U1003, U904 to U1004, U905 to U1005, U906 to U1006, U907 to U1007, USB901 to USB1001, X801 to X901
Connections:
- removed net CLK_MNGR_I2C_SCL: R6.1, U101.B9, U802.4
- removed net CLK_MNGR_I2C_SDA: R5.1, U101.A9, U802.5
- new net !TFT_RESET: U101.H11, U801.10
- new net !TFT_SPI_CS: R805.1, U101.J6, U801.38
- new net !TFT_TOUCH_IRQ: U101.J9, U801.46
- new net !TFT_TOUCH_RESET: U101.J10, U801.47
- new net AUDIO_I2C_SCL: R104.1, U101.A11, U701.12, U702.29
- new net AUDIO_I2C_SDA: R103.1, U101.A10, U701.11, U702.30
- new net N$101: Q802.3, R804.1
- new net N$102: Q801.3, R803.1
- new net N$103: Q801.1, Q802.1, R801.1, R802.2
- new net N$104: SJ1.2, TC201.7
- new net N$20: C424.1, R405.1, R408.1, U403.6
- new net N$21: C427.1, R404.1, R410.1, U403.7
- new net N$23: C507.1, R504.2, U501.10
- new net N$24: R804.2, U801.3
- new net N$25: R803.2, U801.2
- new net SYS_I2C_SCL: R102.1, U101.B9, U801.44, U902.4
- new net SYS_I2C_SDA: R101.1, U101.A9, U801.45, U902.5
- new net TFT_BL_PWM: R801.2, U101.K11
- new net TFT_DC: U101.J11, U801.37
- new net TFT_SPI_MISO: U101.H5, U801.33
- new net TFT_SPI_MOSI: U101.H4, U801.34
- new net TFT_SPI_SCK: U101.J5, U801.36
- new net TXMIXER_TEMP: C510.1, R504.1, U101.H10
- net !CLK_MNGR_IRQ: now also R903.1, U101.C9, U902.3; no longer R803.1, U101.A10, U802.3
- net !CLK_MNGR_OE: now also R902.1, U902.7; no longer R802.1, U802.7
- net !CLK_MNGR_REFCLK_STDBY: now also R901.2, U901.1; no longer R801.2, U801.1
- net !CODEC_RST: now also U101.L11
- net !DSP_RESET: now also R203.1
- net !I2S_BRG_CFG: now also U101.L6
- net !I2S_BRG_RST: now also U101.L8
- net !SMC_RESET: now also R105.1
- net !TXDAC_CS: now also R503.1; no longer R2.1
- net !TXPA_OC: now also R1014.1; no longer R914.1
- net !TXPLL_MUTE: now also R602.2; no longer R4.2
- net 1V2: now also C1006.1, C1007.1, R1003.2, U1002.17; no longer C906.1, C907.1, R903.2, U902.17
- net 1V2_FB: now also R1003.1, R1004.2, U1002.16; no longer R903.1, R904.2, U902.16
- net 1V2_PGOOD: now also R1005.1, U1002.15; no longer R905.1, U902.15
- net 3V3: now also C504.1, C506.1, C901.1, C902.1, C904.1, C905.1, C907.1, R1005.2, R1006.2, R1009.2, R101.2, R1014.2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; no longer C505.1, C508.1, C802.1, C803.1, C805.1, C808.1, R1.2, R2.2, R5.2, R6.2, R802.2, R803.2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
- net 3V3_ANA_RX_CLEAN: now also C411.1, C413.1, C414.1, C421.1; no longer C412.1, C420.1, C422.1, C424.1
- net 3V3_ANA_TX_CLEAN: now also C509.1; no longer C507.1
- net 3V3_FB: now also U1002.11; no longer U902.11
- net 3V3_PGOOD: now also R1009.1, U1002.12; no longer R909.1, U902.12
- net 3V6_ANA: now also R1007.2, U1001.3; no longer R907.2, U901.3
- net 3V6_ANA_FB: now also R1007.1, R1008.2, U1001.4; no longer R907.1, R908.2, U901.4
- net 3V6_ANA_PGOOD: now also R1006.1, U1001.5; no longer R906.1, U901.5
- net 5V0: now also C1001.1, C1002.1, C1003.1, C1004.1, U1001.2, U1001.8, U1001.9, U1002.1, U1002.18, U1002.20, U1002.6, U1002.7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; no longer C901.1, C902.1, C903.1, C904.1, U901.2, U901.8, U901.9, U902.1, U902.18, U902.20, U902.6, U902.7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
- net 5V0_ANA_TXPA_CLEAN: now also C514.1; no longer C510.1
- net DSP_ERASE: now also SJ1.1
- net DSP_MAIN_CLK: now also R906.1; no longer R809.1
- net FPGA_DDC_CLK: now also R905.1; no longer R805.1
- net FPGA_GP_CLK1: now also R907.1; no longer R807.1
- net FPGA_GP_CLK2: now also R904.1; no longer R804.1
- net FPGA_GP_CLK3: now also R908.1; no longer R808.1
- net GND: now also C1001.2, C1002.2, C1003.2, C1004.2, C1005.2, C1006.2, C1007.2, C415.2, C416.2, C417.1, C427.2, C428.2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; no longer C415.1, C417.2, C419.2, C429.2, C508.2, C515.1, C802.2, C803.2, C804.2, C805.2, C807.2, C808.2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
- net N$10: now also C429.2, R413.2, R415.2; no longer C427.2, R409.2, R411.2
- net N$11: now also R907.2, U902.12; no longer R807.2, U802.12
- net N$12: now also R905.2, U902.9; no longer R805.2, U802.9
- net N$13: now also R908.2, U902.8; no longer R808.2, U802.8
- net N$14: now also R909.2, U902.17; no longer R806.2, U802.17
- net N$15: now also C433.2; no longer C431.2
- net N$16: now also C432.2, C433.1; no longer C430.2, C431.1
- net N$17: now also C432.1; no longer C430.1
- net N$19: now also R906.2, U902.16; no longer R809.2, U802.16
- net N$2: now also R506.1; no longer R502.1
- net N$22: now also C423.1, R409.2; no longer C421.1, R406.2
- net N$27: now also C431.1, R414.2; no longer C429.1, R410.2
- net N$3: now also R407.1, R412.1; no longer R405.1, R408.1
- net N$37: now also U1002.4; no longer U902.4
- net N$4: now also C430.1; no longer C428.1
- net N$40: now also U1002.13; no longer U902.13
- net N$41: now also U1002.14; no longer U902.14
- net N$43: now also U1002.3; no longer U902.3
- net N$47: now also R1001.2; no longer R901.2
- net N$49: now also R1002.2; no longer R902.2
- net N$5: now also R406.1, R411.2; no longer R404.1, R407.2
- net N$57: now also C511.2, R507.2; no longer C509.2, R503.2
- net N$6: now also C508.2, C511.1, R506.2; no longer C506.2, C509.1, R502.2
- net N$60: now also U901.4, U902.6; no longer U801.4, U802.6
- net N$61: now also C906.1, U902.2; no longer C807.1, U802.2
- net N$62: now also C903.1, U902.1; no longer C804.1, U802.1
- net N$63: now also C515.2; no longer C513.2
- net N$64: now also C508.1; no longer C506.1
- net N$65: now also U1001.1; no longer U901.1
- net N$66: now also C1005.1, U1001.6; no longer C905.1, U901.6
- net N$67: now also R604.1; no longer R603.1
- net N$69: now also R604.2; no longer R603.2
- net N$7: now also R904.2, U902.13; no longer R804.2, U802.13
- net N$73: now also C517.2, R509.1; no longer C515.2, R505.1
- net N$74: now also C516.1, R508.2; no longer C514.1, R504.2
- net N$75: now also C521.2; no longer C519.2
- net N$76: now also C520.1; no longer C518.1
- net N$77: now also C505.1; no longer C504.1
- net N$78: now also R607.2; no longer R606.2
- net N$79: now also R607.1; no longer R606.1
- net N$8: now also C429.1; no longer C427.1
- net N$80: now also C519.2, R511.1; no longer C517.2, R507.1
- net N$81: now also C518.1, R510.2; no longer C516.1, R506.2
- net N$82: now also C523.2; no longer C521.2
- net N$83: now also C522.1; no longer C520.1
- net N$84: now also R605.1, R606.2; no longer R604.1, R605.2
- net N$88: now also R603.2; no longer R602.2
- net N$9: now also C430.2, R413.1, R416.2; no longer C428.2, R409.1, R412.2
- net N$90: now also C513.2, C515.1; no longer C511.2, C513.1
- net N$92: now also C513.1, R507.1; no longer C511.1, R503.1
- net N$99: now also R605.2; no longer R604.2
- net RXADC_AIN+: now also C419.1, R406.2; no longer C414.1, R404.2
- net RXADC_AIN-: now also C417.2, C419.2, R407.2; no longer C415.2, C416.2, R405.2
- net RXADC_DITH: now also U101.K3
- net RXADC_GAIN: now also U101.L3
- net RXADC_SHDN: now also U101.J4
- net RXADC_VCM: now also C426.1, R411.1, R412.2; no longer C423.1, R407.1, R408.2
- net RXTUNER_DET1: now also C420.1; no longer C417.1
- net RXTUNER_DET2: now also C422.1; no longer C419.1
- net RXTUNER_I2C_SCL: now also R405.2
- net RXTUNER_I2C_SDA: now also R404.2
- net RXTUNER_IFN: now also R416.1; no longer R412.1
- net RXTUNER_IFP: now also R415.1; no longer R411.1
- net RXTUNER_IF_VAGC: now also R414.1; no longer R410.1
- net RXTUNER_PLL_CP: now also C428.1, R409.1; no longer C426.1, R406.1
- net RXTUNER_PLL_VDD: now also C415.1; no longer C413.1
- net RXTUNER_XTALO: now also C412.1; no longer C411.1
- net SMC_MAIN_CLK: now also R909.1; no longer R806.1
- net TXDAC_AUXI: now also R512.2; no longer R508.2
- net TXDAC_AUXQ: now also R513.2; no longer R509.2
- net TXDAC_CLKIN: now also R502.2; no longer R3.2
- net TXDAC_DCLK: now also R502.1; no longer R3.1
- net TXDAC_RESET: now also R505.1; no longer R1.1
- net TXMIXER_IBBN: now also C524.1, R514.2; no longer C522.1, R510.2
- net TXMIXER_IBBP: now also C525.2, R512.1, R514.1; no longer C523.2, R508.1, R510.1
- net TXMIXER_QBBN: now also C526.1, R515.2; no longer C524.1, R511.2
- net TXMIXER_QBBP: now also C527.2, R513.1, R515.1; no longer C525.2, R509.1, R511.1
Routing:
- net 3V3: track 187.7 -> 445.5 mm, vias 77 -> 107
- net !TXDAC_CS: track 0.00 -> 166.6 mm, vias 0 -> 4
- net TXDAC_SDIO: track 0.00 -> 162.9 mm, vias 0 -> 4
- net TXDAC_RESET: track 0.00 -> 162.6 mm, vias 0 -> 4
- net TXDAC_SCLK: track 0.00 -> 162.5 mm, vias 0 -> 4
- net TXPA_BIAS_EN: track 0.00 -> 156.9 mm, vias 0 -> 4
- net N$23: track 0.00 -> 149.6 mm, vias 0 -> 6
- net !TXPA_OC: track 0.00 -> 149.5 mm, vias 0 -> 4
- net TXMIXER_EN: track 0.00 -> 131.7 mm, vias 0 -> 5
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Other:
- board text added: "IcyRadio v1 Oct 2019"
